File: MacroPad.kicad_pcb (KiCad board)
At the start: 2 copper layers, 111.1 x 120.1 mm, 56 parts, among them J1 AVR-ISP-6, SW1 Rotary_Encoder_Switch, SW10 *, SW11 9, SW12 6, SW13 3, SW14 ., SW15 -, SW16 +, SW17 Enter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

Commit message: cambiando rutas
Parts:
- moved C3 70.7 mm to (54.2, 65.3), turned to 135 degrees
- moved R1 60.6 mm to (119.3, 72.4)
- moved F1 60.6 mm to (108.3, 78.9)
- moved USB1 60.6 mm to (113.8, 60.5)
- moved R2 60.6 mm to (108.2, 72.4)
- moved U2 60.6 mm to (113.9, 76.4)
- moved J1 37.6 mm to (124.8, 67.6), turned to 90 degrees
- moved C2 30.8 mm to (127.4, 99.4), turned to 135 degrees
- moved C5 27.8 mm to (120.8, 92.6), turned to 315 degrees
- moved D17 23.8 mm to (147.6, 111.9)
- moved C4 21.0 mm to (140.1, 93.2), turned to 45 degrees
- moved R6 20.8 mm to (133.7, 99.8), turned to 45 degrees
- moved D11 19.7 mm to (126.2, 142.2)
- moved D14 18.8 mm to (126.4, 111.9)
- moved C6 13.9 mm to (144.9, 79.5), turned to 45 degrees
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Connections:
- net sw14 renamed Net-(D13-Pad1)
- net sw17 renamed Net-(D16-Pad1)
- net sw5 renamed Net-(D4-Pad1)
- net sw8 renamed Net-(D7-Pad1)
- net sw9 renamed Net-(D8-Pad1)
- D1 pad 1: sw2 -> Net-(D1-Pad1)
- D1 pad 2: row1 -> ROW1
- D10 pad 1: sw11 -> Net-(D10-Pad1)
- D10 pad 2: row1 -> ROW1
- D11 pad 1: sw12 -> Net-(D11-Pad1)
- D11 pad 2: row2 -> ROW2
- D12 pad 1: sw13 -> Net-(D12-Pad1)
- D12 pad 2: row3 -> ROW3
- D13 pad 2: row4 -> ROW4
- D14 pad 1: sw15 -> Net-(D14-Pad1)
- D14 pad 2: row0 -> ROW0
- D15 pad 1: sw16 -> Net-(D15-Pad1)
- D15 pad 2: row1 -> ROW1
- D16 pad 2: row4 -> ROW4
- D17 pad 1: S2 -> Net-(D17-Pad1)
- D17 pad 2: row0 -> ROW0
- D2 pad 1: sw3 -> Net-(D2-Pad1)
- D2 pad 2: row2 -> ROW2
- D3 pad 1: sw4 -> Net-(D3-Pad1)
- D3 pad 2: row3 -> ROW3
- D4 pad 2: row4 -> ROW4
- D5 pad 1: sw6 -> Net-(D5-Pad1)
- D5 pad 2: row0 -> ROW0
- D6 pad 1: sw7 -> Net-(D6-Pad1)
- D6 pad 2: row1 -> ROW1
- D7 pad 2: row2 -> ROW2
- D8 pad 2: row3 -> ROW3
- D9 pad 1: sw10 -> Net-(D9-Pad1)
- D9 pad 2: row0 -> ROW0
- SW1 pad S1: col0 -> col3
- SW1 pad S2: S2 -> Net-(D14-Pad1)
- SW10 pad 1: sw10 -> Net-(D5-Pad1)
- SW10 pad 2: col2 -> col1
- SW11 pad 1: sw11 -> Net-(D1-Pad1)
- SW11 pad 2: col2 -> col1
- SW12 pad 1: sw12 -> Net-(D2-Pad1)
- SW12 pad 2: col2 -> col1
- SW13 pad 1: sw13 -> Net-(D3-Pad1)
- SW13 pad 2: col2 -> col1
- SW14 pad 2: col2 -> col1
- SW15 pad 1: sw15 -> Net-(D17-Pad1)
- SW15 pad 2: col3 -> col0
- SW16 pad 1: sw16 -> Net-(D6-Pad1)
- SW16 pad 2: col3 -> col0
- SW17 pad 2: col3 -> col0
- SW2 pad 1: sw2 -> Net-(D15-Pad1)
- SW2 pad 2: col0 -> col3
- SW3 pad 1: sw3 -> Net-(D11-Pad1)
- SW3 pad 2: col0 -> col3
- SW4 pad 1: sw4 -> Net-(D12-Pad1)
- SW4 pad 2: col0 -> col3
- SW5 pad 2: col0 -> col3
- SW6 pad 1: sw6 -> Net-(D9-Pad1)
- SW6 pad 2: col1 -> col2
- SW7 pad 1: sw7 -> Net-(D10-Pad1)
- SW7 pad 2: col1 -> col2
- SW8 pad 2: col1 -> col2
- SW9 pad 2: col1 -> col2
- U1 pad 1: hwb -> Net-(U1-Pad1)
- U1 pad 10: Net-(U1-Pad10) -> mosi
- U1 pad 11: Net-(U1-Pad11) -> sck
- U1 pad 12: Net-(U1-Pad12) -> miso
- U1 pad 25: miso -> Net-(U1-Pad25)
- U1 pad 26: sck -> Net-(U1-Pad26)
- U1 pad 27: mosi -> Net-(U1-Pad27)
- U1 pad 28: Net-(U1-Pad28) -> ROW4
- U1 pad 29: row4 -> ROW3
- U1 pad 30: row3 -> ROW2
- U1 pad 31: row2 -> ROW1
- U1 pad 32: row1 -> ROW0
- U1 pad 33: row0 -> hwb
- U1 pad 36: col0 -> col3
- U1 pad 37: col1 -> col2
- U1 pad 38: col2 -> col1
- U1 pad 39: col3 -> col0
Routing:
- net GND: track 336.6 -> 137.2 mm, vias 2 -> 0
- net col0: track 224.2 -> 82.5 mm, vias 7 -> 4
- net sw2: track 121.3 -> 0.00 mm
- net Net-(D12-Pad1): track 0.00 -> 107.6 mm
- net row4: track 107.2 -> 0.00 mm
- net ROW4: track 0.00 -> 104.6 mm
- net sw3: track 103.6 -> 0.00 mm
- net Net-(D15-Pad1): track 0.00 -> 103.3 mm
- net Net-(D11-Pad1): track 0.00 -> 98.6 mm
- net col1: track 221.6 -> 123.6 mm, vias 9 -> 8
- net Net-(D14-Pad1): track 0.00 -> 97.7 mm
- net sw7: track 97.1 -> 0.00 mm
- net sw4: track 95.5 -> 0.00 mm
- net Net-(D9-Pad1): track 0.00 -> 94.6 mm
- net sw6: track 92.8 -> 0.00 mm
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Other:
- board outline removed

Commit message: ultimas partes
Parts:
- added FB1: 60@100Mhz, Inductor_SMD:L_0805_2012Metric_Pad1.15x1.40mm_HandSolder, B.Cu at (117.2, 52.1)
- moved C3 84.6 mm to (138.8, 66.5)
- moved D13 19.7 mm to (146.3, 156.6)
- moved D7 19.7 mm to (146.3, 127.2)
- moved D8 19.7 mm to (146.3, 142.3)
- moved C4 19.7 mm to (152.8, 78.1)
- moved D1 19.7 mm to (160.3, 111.9)
- moved D10 19.7 mm to (146.3, 111.9)
- moved D11 19.7 mm to (138.9, 127.2)
- moved D17 19.7 mm to (160.3, 96.8)
- moved D3 19.7 mm to (139.1, 142.3)
- moved D4 19.7 mm to (139.1, 156.6)
- moved D9 19.7 mm to (146.3, 96.8)
- moved SW12 19.7 mm to (100.8, 115.1)
- moved SW14 19.7 mm to (100.8, 153.2)
- moved SW16 19.7 mm to (119.9, 105.6)
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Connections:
- U1 pad 21: Net-(U1-Pad21) -> sda
- U1 pad 22: Net-(U1-Pad22) -> scl
- U1 pad 28: ROW4 -> ROW0
- U1 pad 29: ROW3 -> ROW1
- U1 pad 31: ROW1 -> ROW3
- U1 pad 32: ROW0 -> ROW4
- U1 pad 8: scl -> Net-(U1-Pad8)
- U1 pad 9: sda -> Net-(U1-Pad9)
- USB1 pad 13: GND -> Earth
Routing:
- net en2: track 0.00 -> 108.0 mm
- net en1: track 0.00 -> 101.5 mm
- net GND: track 137.2 -> 220.0 mm, vias 0 -> 7
- net sda: track 0.00 -> 74.7 mm, vias 0 -> 2
- net scl: track 0.00 -> 71.7 mm, vias 0 -> 2
- net ROW4: track 104.6 -> 89.7 mm
- net ROW2: track 75.3 -> 60.8 mm
- net ROW3: track 88.9 -> 75.5 mm
- net VCC: track 24.6 -> 35.8 mm
- net ROW1: track 60.1 -> 52.5 mm
- net Earth: track 0.00 -> 7.42 mm, vias 0 -> 3
- net D+: track 8.38 -> 9.76 mm
- net ROW0: track 36.8 -> 37.9 mm
- net D-: track 8.11 -> 9.09 mm
- net +5V: track 137.9 -> 138.8 mm
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- added copper zone on B.Cu, net Earth
- added copper zone on F.Cu, net Earth
- added copper zone on B.Cu, net GND
- added copper zone on F.Cu, net GND
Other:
- board outline added: 123.8 x 122.6 mm

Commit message: final final
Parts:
- SW10, SW11, SW12, SW13, SW14, SW15, SW2, SW3, SW4, SW6, SW7, SW8, SW9: footprint kailh MX:Kailh_socket_MX -> kailh_switches:SW_Hotswap_Kailh_1.00u
- SW16, SW17: footprint kailh MX:Kailh_socket_MX -> kailh_switches:SW_Hotswap_Kailh_2.00u_Rotated
- SW5: footprint kailh MX:Kailh_socket_MX -> kailh_switches:SW_Hotswap_Kailh_2.00u

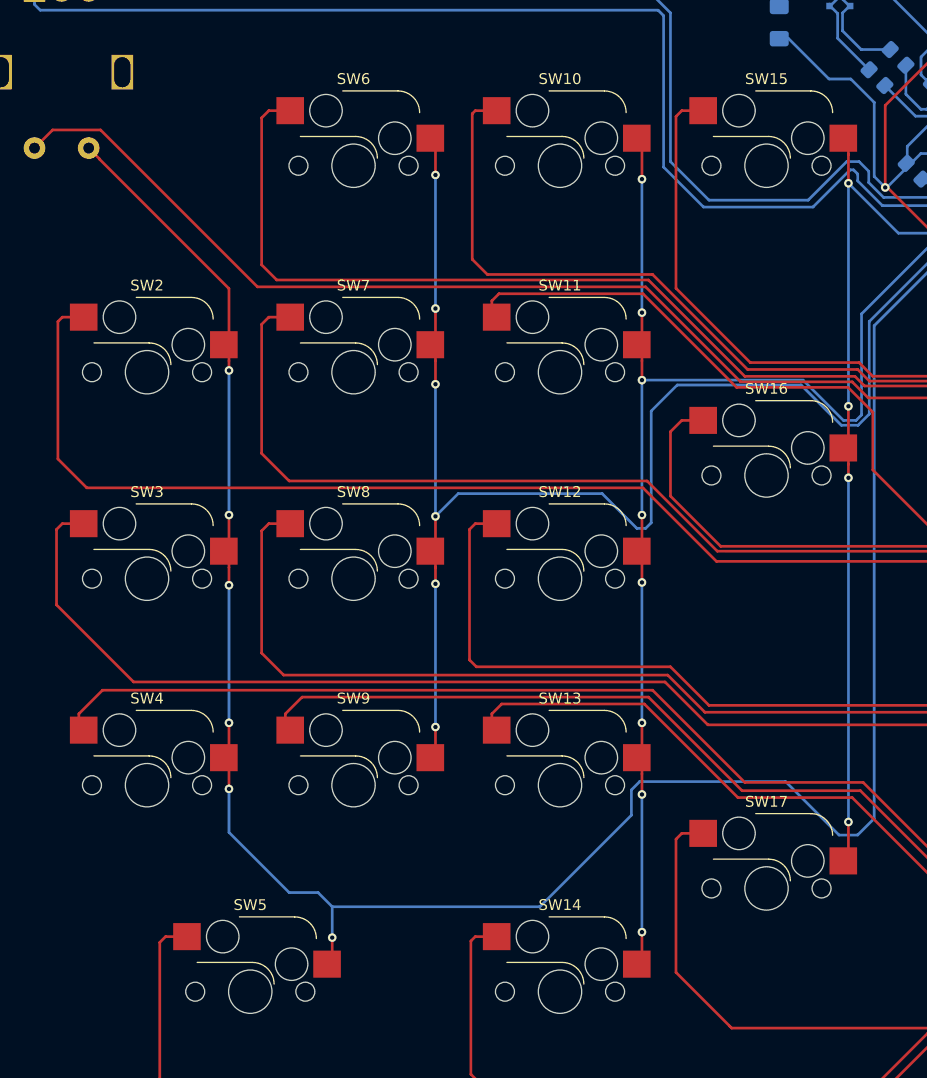
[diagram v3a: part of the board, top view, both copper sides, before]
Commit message: cambio de footprint
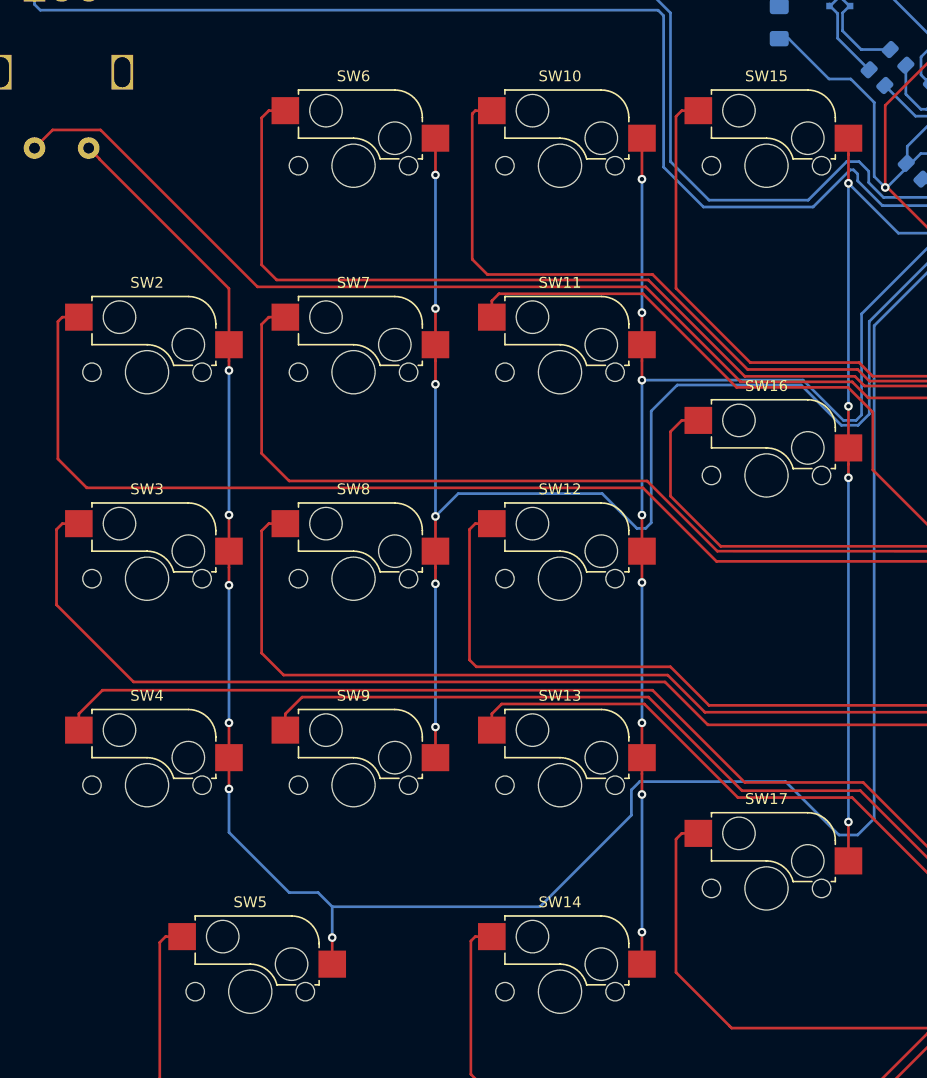
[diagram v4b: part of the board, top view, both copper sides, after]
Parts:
- SW10, SW11, SW12, SW13, SW14, SW15, SW2, SW3, SW4, SW6, SW7, SW8, SW9: footprint kailh_switches:SW_Hotswap_Kailh_1.00u -> kailh MX:Kailh_socket_MX
- SW16, SW17: footprint kailh_switches:SW_Hotswap_Kailh_2.00u_Rotated -> kailh MX:Kailh_socket_MX
- SW5: footprint kailh_switches:SW_Hotswap_Kailh_2.00u -> kailh MX:Kailh_socket_MX

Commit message: cambiado tamaño pistas y vcc oled
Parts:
- moved SW1 5.61 mm to (56.3, 64.8)
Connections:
- OL1 pad 2: VCC -> +5V
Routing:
- net +5V: track 138.8 -> 159.0 mm, vias 6 -> 7
- net VCC: track 35.8 -> 25.4 mm
- net col3: track 206.5 -> 200.9 mm
- net Net-(D14-Pad1): track 97.7 -> 93.3 mm
- net GND: track 220.0 -> 217.2 mm
- net en1: track 101.5 -> 99.1 mm
- net en2: track 108.0 -> 106.3 mm
